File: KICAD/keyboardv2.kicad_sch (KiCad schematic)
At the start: 333 parts, among them SW1 RotaryEncoder_Switch_MP

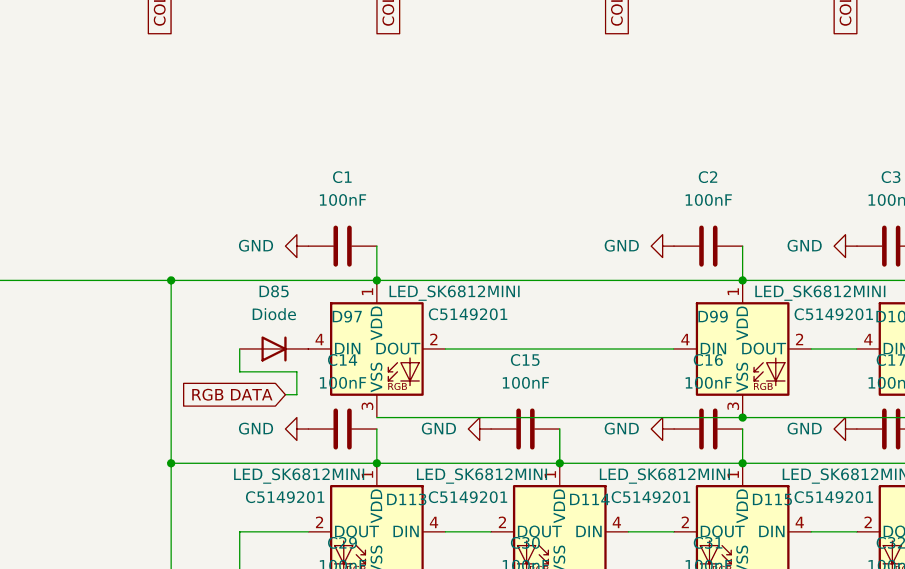
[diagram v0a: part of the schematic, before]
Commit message: Fixed Fatal Flaw in RGB LED Data Line, Updated BOM
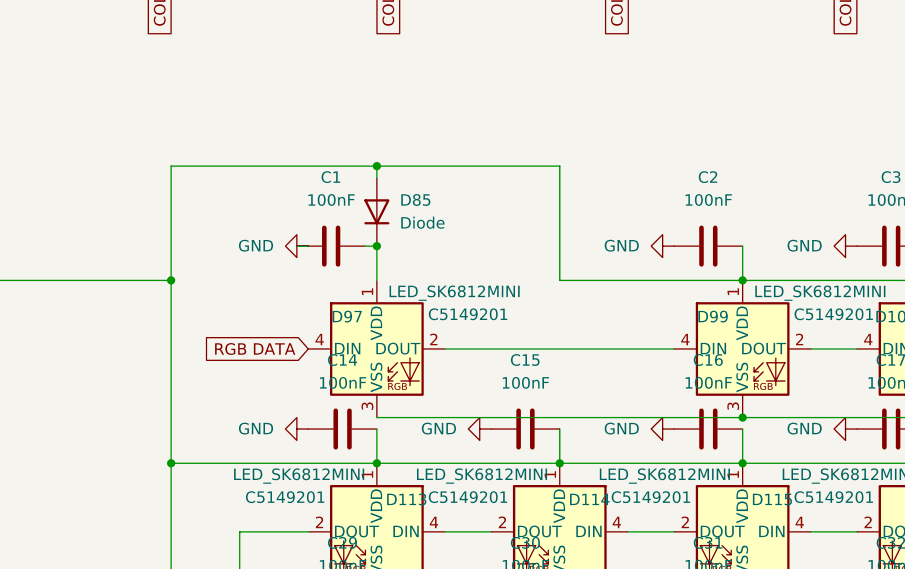
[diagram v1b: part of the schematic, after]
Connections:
- net RGB DATA: now also D97.4 (DIN); no longer D85.2 (A)
- net VBUS: now also D85.2 (A); no longer C1.2, D97.1 (VDD)
- net at D85.1 (K): now also C1.2, D97.1 (VDD); no longer D97.4 (DIN)
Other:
- moved on the sheet: C1, D85
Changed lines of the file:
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@@
 	)
 	(junction
-		(at 125.73 148.59)
-		(diameter 0)
-		(color 0 0 0 0)
-	)
-	(junction
 		(at 308.61 245.11)
 		(diameter 0)
@@
 	)
 	(junction
+		(at 125.73 144.78)
+		(diameter 0)
+		(color 0 0 0 0)
+	)
+	(junction
 		(at 228.6 81.28)
 		(diameter 0)
@@
 	)
 	(junction
+		(at 125.73 135.89)
+		(diameter 0)
+		(color 0 0 0 0)
+	)
+	(junction
 		(at 267.97 168.91)
 		(diameter 0)
@@
 	(wire
 		(pts
-			(xy 116.84 158.75) (xy 116.84 161.29)
-		)
-		(stroke
-			(width 0)
-			(type default)
-		)
-	)
-	(wire
-		(pts
 			(xy 267.97 148.59) (xy 288.29 148.59)
 		)
@@
 	(wire
 		(pts
-			(xy 102.87 148.59) (xy 125.73 148.59)
+			(xy 102.87 135.89) (xy 125.73 135.89)
 		)
 		(stroke
@@
 	(wire
 		(pts
+			(xy 102.87 135.89) (xy 102.87 148.59)
+		)
+		(stroke
+			(width 0)
+			(type default)
+		)
+	)
+	(wire
+		(pts
 			(xy 124.46 229.87) (xy 125.73 229.87)
 		)
@@
 	(wire
 		(pts
-			(xy 125.73 148.59) (xy 166.37 148.59)
-		)
-		(stroke
-			(width 0)
-			(type default)
-		)
-	)
-	(wire
-		(pts
 			(xy 336.55 237.49) (xy 361.95 237.49)
 		)
@@
 	(wire
 		(pts
-			(xy 125.73 144.78) (xy 125.73 148.59)
-		)
-		(stroke
-			(width 0)
-			(type default)
-		)
-	)
-	(wire
-		(pts
 			(xy 186.69 184.15) (xy 207.01 184.15)
 		)
@@
 	(wire
 		(pts
+			(xy 125.73 135.89) (xy 146.05 135.89)
+		)
+		(stroke
+			(width 0)
+			(type default)
+		)
+	)
+	(wire
+		(pts
 			(xy 316.23 176.53) (xy 321.31 176.53)
 		)
@@
 	(wire
 		(pts
+			(xy 125.73 144.78) (xy 125.73 148.59)
+		)
+		(stroke
+			(width 0)
+			(type default)
+		)
+	)
+	(wire
+		(pts
 			(xy 228.6 81.28) (xy 228.6 93.98)
 		)
@@
 	(wire
 		(pts
-			(xy 115.57 161.29) (xy 116.84 161.29)
-		)
-		(stroke
-			(width 0)
-			(type default)
-		)
-	)
-	(wire
-		(pts
 			(xy 173.99 156.21) (xy 179.07 156.21)
 		)
@@
 	(wire
 		(pts
-			(xy 110.49 156.21) (xy 110.49 158.75)
-		)
-		(stroke
-			(width 0)
-			(type default)
-		)
-	)
-	(wire
-		(pts
 			(xy 266.7 38.1) (xy 292.1 38.1)
 		)
@@
 	(wire
 		(pts
-			(xy 110.49 158.75) (xy 116.84 158.75)
-		)
-		(stroke
-			(width 0)
-			(type default)
-		)
-	)
-	(wire
-		(pts
 			(xy 328.93 185.42) (xy 328.93 189.23)
 		)
@@
 	(wire
 		(pts
+			(xy 146.05 135.89) (xy 146.05 148.59)
+		)
+		(stroke
+			(width 0)
+			(type default)
+		)
+	)
+	(wire
+		(pts
 			(xy 288.29 224.79) (xy 308.61 224.79)
 		)
@@
 	(wire
 		(pts
+			(xy 146.05 148.59) (xy 166.37 148.59)
+		)
+		(stroke
+			(width 0)
+			(type default)
+		)
+	)
+	(wire
+		(pts
 			(xy 279.4 81.28) (xy 279.4 93.98)
 		)
@@
 	(wire
 		(pts
+			(xy 124.46 144.78) (xy 125.73 144.78)
+		)
+		(stroke
+			(width 0)
+			(type default)
+		)
+	)
+	(wire
+		(pts
 			(xy 308.61 209.55) (xy 288.29 209.55)
 		)
@@
 	(wire
 		(pts
+			(xy 125.73 135.89) (xy 125.73 137.16)
+		)
+		(stroke
+			(width 0)
+			(type default)
+		)
+	)
+	(wire
+		(pts
 			(xy 166.37 204.47) (xy 186.69 204.47)
 		)
@@
 	(wire
 		(pts
+			(xy 116.84 144.78) (xy 118.11 144.78)
+		)
+		(stroke
+			(width 0)
+			(type default)
+		)
+	)
+	(wire
+		(pts
 			(xy 267.97 205.74) (xy 267.97 209.55)
 		)
@@
 	(global_label "RGB DATA"
 		(shape input)
-		(at 115.57 161.29 180)
+		(at 118.11 156.21 180)
 		(fields_autoplaced yes)
 		(effects
@@
 		)
 		(property "Intersheetrefs" "${INTERSHEET_REFS}"
-			(at 103.3924 161.29 0)
+			(at 105.9324 156.21 0)
 			(effects
 				(font
@@
 	(symbol
 		(lib_id "Device:C")
-		(at 121.92 144.78 90)
+		(at 120.65 144.78 90)
 		(unit 1)
 		(exclude_from_sim no)
@@
 		(fields_autoplaced yes)
 		(property "Reference" "C1"
-			(at 121.92 137.16 90)
+			(at 120.65 137.16 90)
 			(effects
 				(font
@@
 		)
 		(property "Value" "100nF"
-			(at 121.92 139.7 90)
+			(at 120.65 139.7 90)
 			(effects
 				(font
@@
 		)
 		(property "Footprint" "Capacitor_SMD:C_0402_1005Metric"
-			(at 125.73 143.8148 0)
+			(at 124.46 143.8148 0)
 			(effects
 				(font
@@
 		)
 		(property "Datasheet" "~"
-			(at 121.92 144.78 0)
+			(at 120.65 144.78 0)
 			(effects
 				(font
@@
 		)
 		(property "Description" "Unpolarized capacitor"
-			(at 121.92 144.78 0)
+			(at 120.65 144.78 0)
 			(effects
 				(font
@@
 	(symbol
 		(lib_id "Scottokicad:Placeholder_Diode")
-		(at 114.3 156.21 180)
+		(at 125.73 140.97 90)
 		(unit 1)
 		(exclude_from_sim no)
@@
 		(fields_autoplaced yes)
 		(property "Reference" "D85"
-			(at 114.3 149.86 0)
+			(at 128.27 139.6999 90)
 			(effects
 				(font
 					(size 1.27 1.27)
 				)
+				(justify right)
 			)
 		)
 		(property "Value" "Diode"
-			(at 114.3 152.4 0)
+			(at 128.27 142.2399 90)
 			(effects
 				(font
 					(size 1.27 1.27)
 				)
+				(justify right)
 			)
 		)
 		(property "Footprint" "Diode_SMD:D_SOD-123"
-			(at 114.3 156.21 0)
+			(at 125.73 140.97 0)
 			(effects
 				(font
@@
 		)
 		(property "Datasheet" ""
-			(at 114.3 156.21 0)
+			(at 125.73 140.97 0)
 			(effects
 				(font
@@
 		)
 		(property "Description" "1N4148 (DO-35) or 1N4148W (SOD-123)"
-			(at 114.3 156.21 0)
+			(at 125.73 140.97 0)
 			(effects
 				(font
@@
 		)
 		(property "Sim.Device" "D"
-			(at 114.3 156.21 0)
+			(at 125.73 140.97 0)
 			(effects
 				(font
@@
 		)
 		(property "Sim.Pins" "1=K 2=A"
-			(at 114.3 156.21 0)
+			(at 125.73 140.97 0)
 			(effects
 				(font
